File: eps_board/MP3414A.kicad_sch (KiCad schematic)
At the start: 9 parts, among them U84 MP3414A

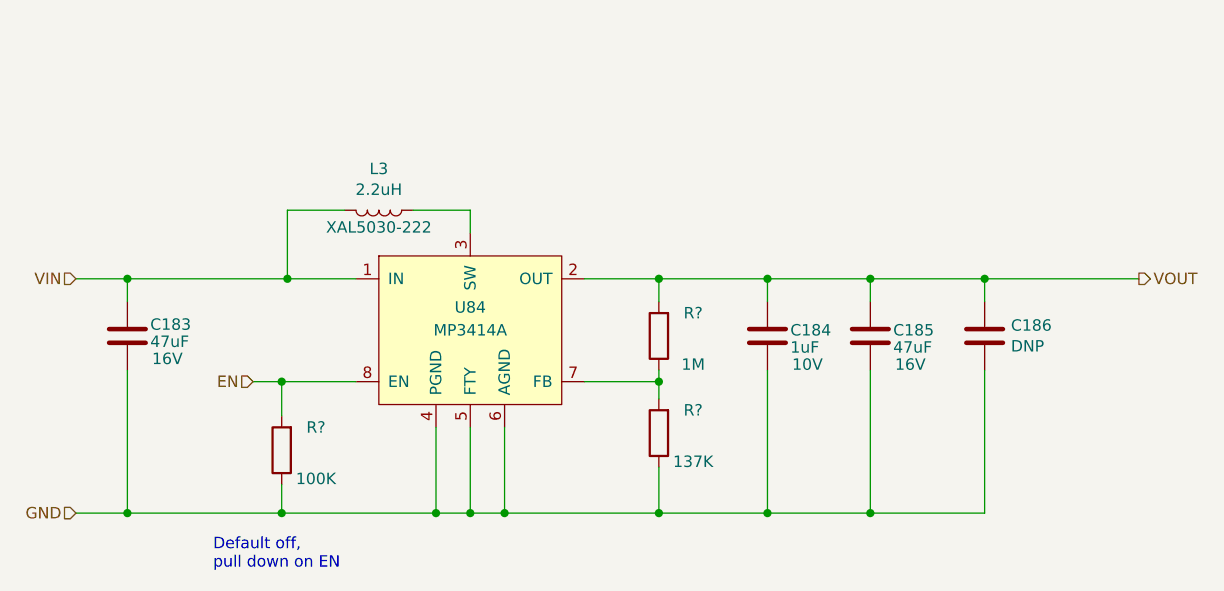
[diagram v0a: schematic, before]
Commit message: EPS: cleaning up, footprint to 80x80, and replace discrete switches with ICs for switch and measurement
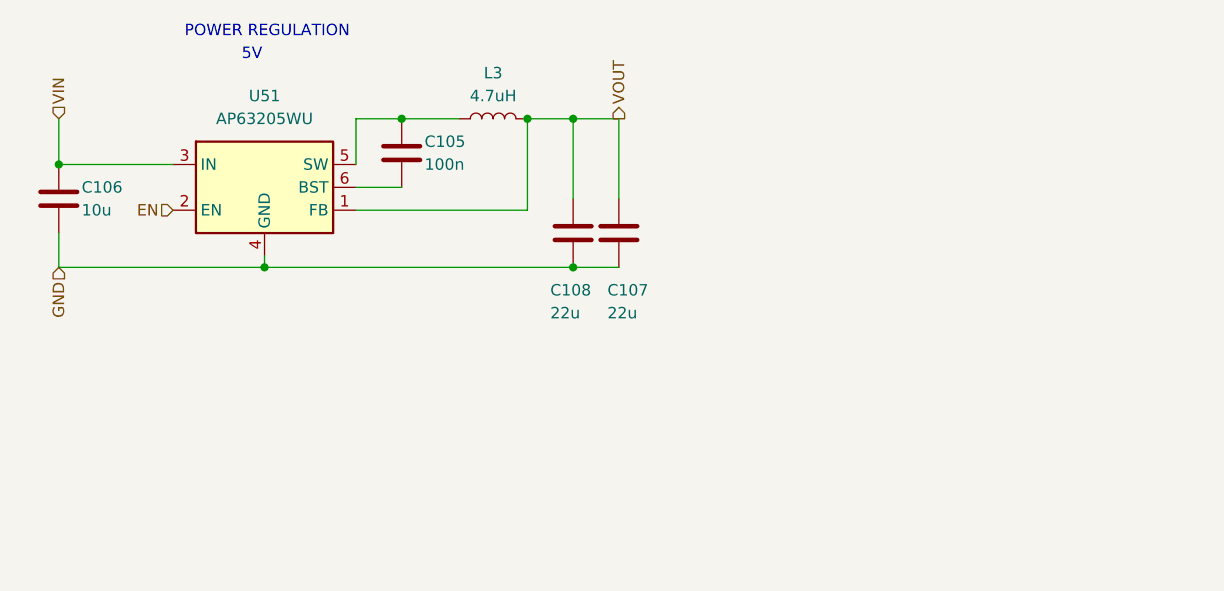
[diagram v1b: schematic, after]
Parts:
- removed C183, C185: 47uF, Capacitor_SMD:C_1210_3225Metric_Pad1.42x2.65mm_HandSolder, symbol Device:C
- removed C184: 1uF, Capacitor_SMD:C_0603_1608Metric_Pad1.05x0.95mm_HandSolder, symbol Device:C
- removed C186: DNP, Capacitor_SMD:C_1210_3225Metric_Pad1.42x2.65mm_HandSolder, symbol Device:C
- removed R?: 1M, Resistor_SMD:R_0603_1608Metric_Pad1.05x0.95mm_HandSolder, symbol Device:R
- removed R?: 137K, Resistor_SMD:R_0603_1608Metric_Pad1.05x0.95mm_HandSolder, symbol Device:R
- removed R?: 100K, Resistor_SMD:R_0603_1608Metric_Pad1.05x0.95mm_HandSolder, symbol Device:R
- removed U84: MP3414A, Package_TO_SOT_SMD:TSOT-23-8_HandSoldering, symbol EPS-rescue:MP3414A-1K_Custom_Symbol
- added C105: 100n, Capacitor_SMD:C_0402_1005Metric_Pad0.74x0.62mm_HandSolder, symbol Device:C
- added C106: 10u, Capacitor_SMD:C_0603_1608Metric_Pad1.08x0.95mm_HandSolder, symbol Device:C
- added C107, C108: 22u, Capacitor_SMD:C_0805_2012Metric_Pad1.18x1.45mm_HandSolder, symbol Device:C
- added U51: AP63205WU, Package_TO_SOT_SMD:TSOT-23-6_HandSoldering, symbol Regulator_Switching:AP63205WU
- L3: value 2.2uH -> 4.7uH; footprint Inductor_SMD:L_Coilcraft_XAL5030 -> Inductor_SMD:L_1210_3225Metric_Pad1.42x2.65mm_HandSolder; Amps (none) -> 2; Manufactorer (none) -> Murata; Mfr. # XAL5030-222 -> (none); Order https://www.coilcraft.com/en-us/products/power/shielded-ind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 -> (none); Part Number (none) -> DFE322520FD-4R7M=P2; Tolerance (none) -> 20%
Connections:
- net EN: now also U51.2 (EN)
- net GND: now also C106.2, C107.2, C108.2, U51.4 (GND)
- net VIN: now also C106.1, U51.3 (IN); no longer L3.2
- net VOUT: now also L3.2, C107.1, C108.1, U51.1 (FB)
- net at L3.1: now also C105.1, U51.5 (SW)
- new net: C105.2, U51.6 (BST)
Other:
- note added: "5V"
- note added: "POWER REGULATION"
- note removed: "Default off, pull down on EN"

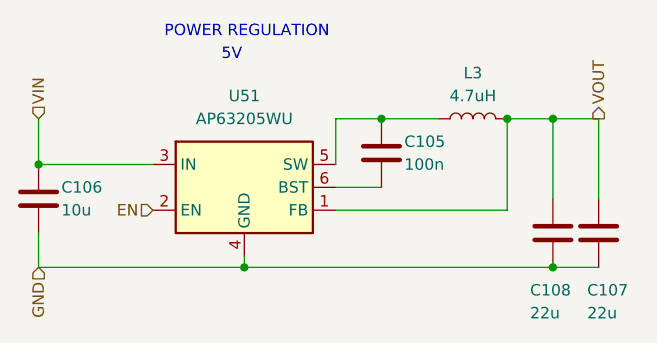
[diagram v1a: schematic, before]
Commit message: combine interrupts per powerline and use i2c expanders to turn on and solicit feedback
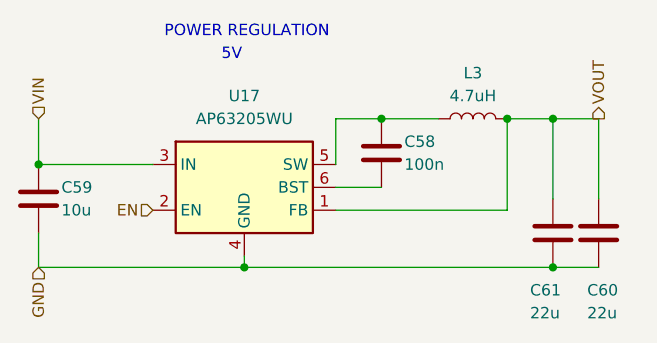
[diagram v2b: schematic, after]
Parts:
- renumbered C105 to C58, C106 to C59, C107 to C60, C108 to C61, U51 to U17
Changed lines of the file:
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@@
 		(on_board yes)
 		(dnp no)
-		(property "Reference" "C106"
+		(property "Reference" "C59"
 			(at 96.52 83.82 0)
 			(effects
@@
 			(project "EPS"
 				(path "/05170af6-30ef-4c3a-b972-f098085da1bc/00000000-0000-0000-0000-00005f8870a6"
-					(reference "C106")
+					(reference "C59")
 					(unit 1)
 				)
@@
 		(on_board yes)
 		(dnp no)
-		(property "Reference" "C105"
+		(property "Reference" "C58"
 			(at 134.62 78.74 0)
 			(effects
@@
 			(project "EPS"
 				(path "/05170af6-30ef-4c3a-b972-f098085da1bc/00000000-0000-0000-0000-00005f8870a6"
-					(reference "C105")
+					(reference "C58")
 					(unit 1)
 				)
@@
 		(dnp no)
 		(fields_autoplaced yes)
-		(property "Reference" "U51"
+		(property "Reference" "U17"
 			(at 116.84 73.66 0)
 			(effects
@@
 			(project "EPS"
 				(path "/05170af6-30ef-4c3a-b972-f098085da1bc/00000000-0000-0000-0000-00005f8870a6"
-					(reference "U51")
+					(reference "U17")
 					(unit 1)
 				)
@@
 		(on_board yes)
 		(dnp no)
-		(property "Reference" "C107"
+		(property "Reference" "C60"
 			(at 154.94 95.25 0)
 			(effects
@@
 			(project "EPS"
 				(path "/05170af6-30ef-4c3a-b972-f098085da1bc/00000000-0000-0000-0000-00005f8870a6"
-					(reference "C107")
+					(reference "C60")
 					(unit 1)
 				)
@@
 		(on_board yes)
 		(dnp no)
-		(property "Reference" "C108"
+		(property "Reference" "C61"
 			(at 148.59 95.25 0)
 			(effects
@@
 			(project "EPS"
 				(path "/05170af6-30ef-4c3a-b972-f098085da1bc/00000000-0000-0000-0000-00005f8870a6"
-					(reference "C108")
-					(unit 1)
-				)
+					(reference "C61")
+					(unit 1)
+				)
